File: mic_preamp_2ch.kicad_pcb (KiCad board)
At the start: 2 copper layers, 100 x 78 mm, 47 parts, among them J1 NC3FAH1, J2 NC3FAH1, J3 PWR +15/GND/-15, J4 P48 +48/GND, J5 OUT1/GND/OUT2/GND, U1 INA163UA, U2 INA163UA

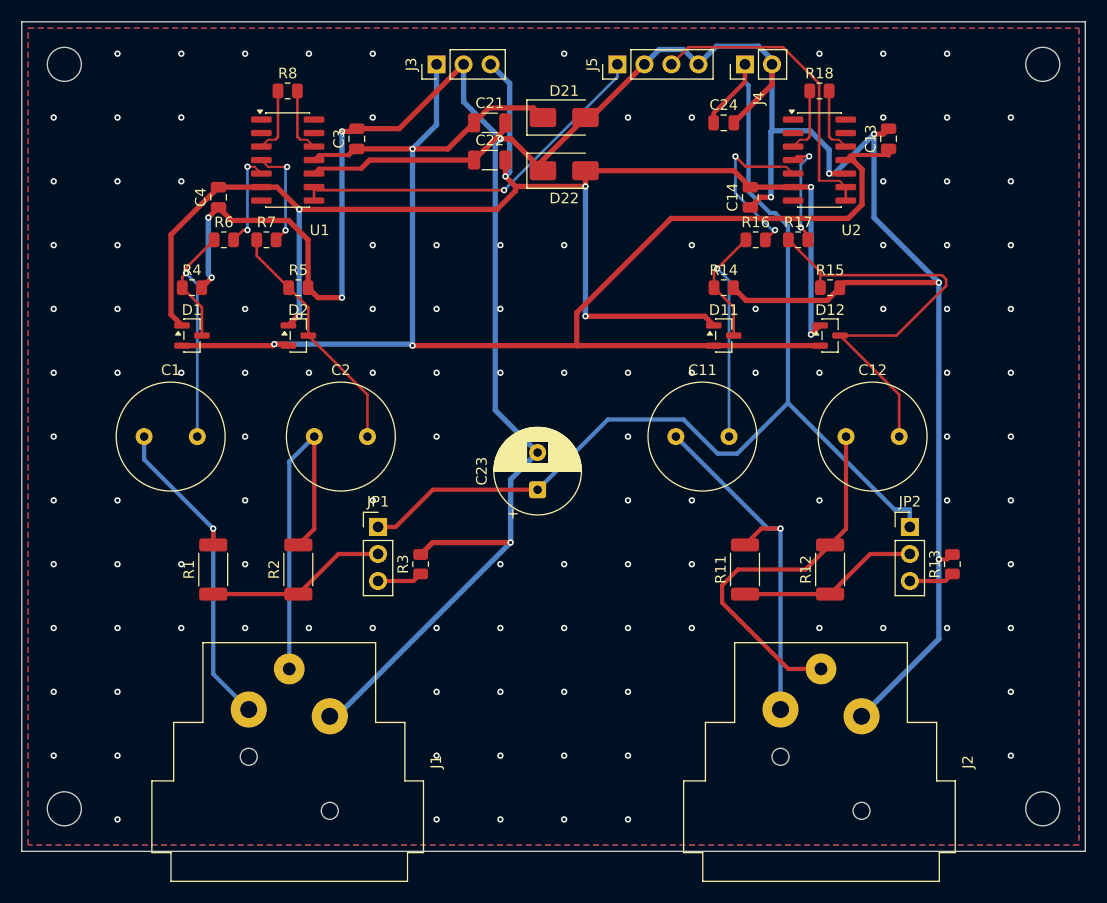
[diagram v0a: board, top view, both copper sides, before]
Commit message: v2: hand-routed symmetric input path, 0.1% matched parts, 10R series
Fixes the review of efc1e58: the 47R series resistors were a misreading of
datasheet Fig.2 (47R is in parallel with 1.2uH there) and doubled input noise.
Phantom feed is now 2x3.40k 0.1% per leg, bias 2.2k 0.1%, series 10R.
Input legs are routed by hand and locked; only power/phantom/GND autorouted.
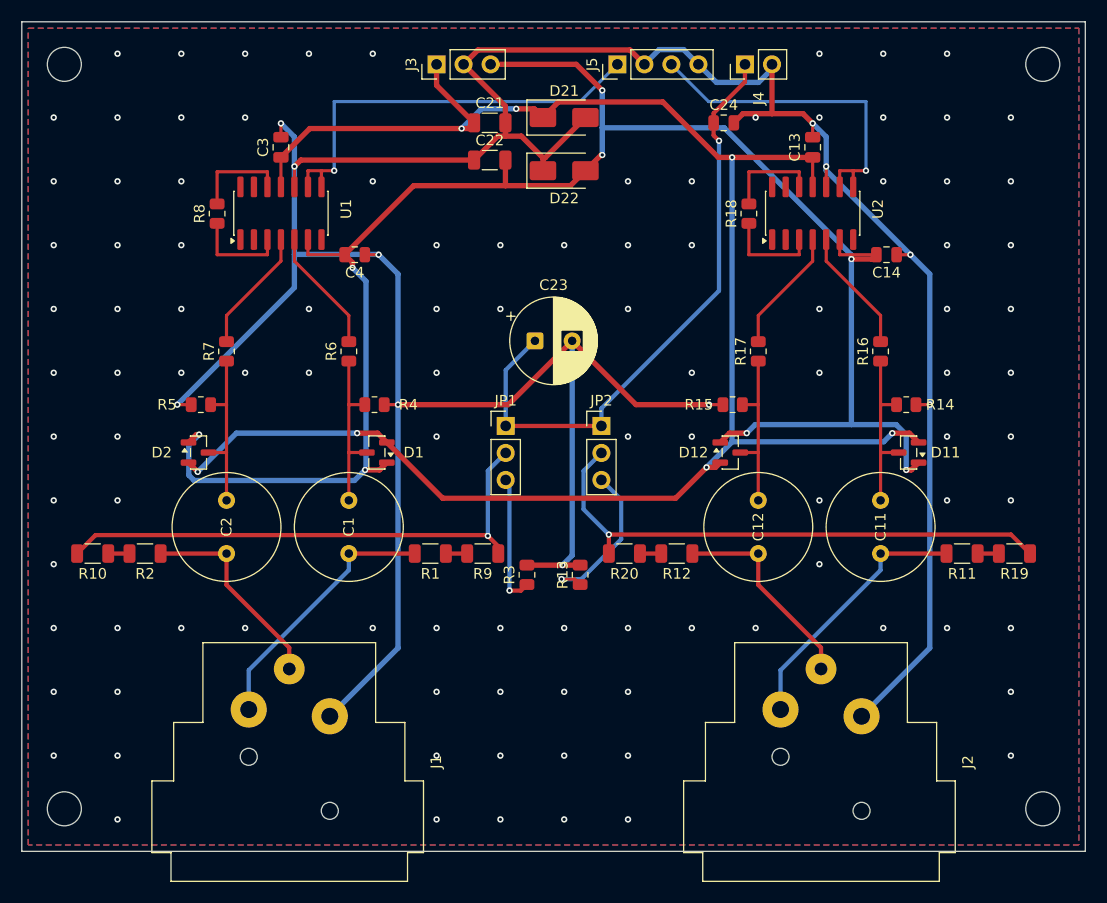
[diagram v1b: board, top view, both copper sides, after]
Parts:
- added R10: 3.40k, Resistor_SMD:R_1206_3216Metric, F.Cu at (6.66, 50.0)
- added R19: 3.40k, Resistor_SMD:R_1206_3216Metric, F.Cu at (93.3, 50.0)
- added R20: 3.40k, Resistor_SMD:R_1206_3216Metric, F.Cu at (56.7, 50.0)
- added R9: 3.40k, Resistor_SMD:R_1206_3216Metric, F.Cu at (43.3, 50.0)
- R1, R11, R12, R2: value 6.81k -> 3.40k; footprint Resistor_SMD:R_2010_5025Metric -> Resistor_SMD:R_1206_3216Metric
- R16, R17, R6, R7: value 47R -> 10R
- moved R13 35.0 mm to (52.5, 52.0)
- moved JP2 30.5 mm to (54.5, 38.0)
- moved C1 22.2 mm to (30.8, 50.0), turned to 90 degrees
- moved C11 22.2 mm to (80.8, 50.0), turned to 90 degrees
- moved D1 20.6 mm to (33.4, 40.5), turned to 180 degrees
- moved D11 20.6 mm to (83.4, 40.5), turned to 180 degrees
- moved R1 20.5 mm to (38.4, 50.0), turned to 180 degrees
- moved R11 20.5 mm to (88.4, 50.0), turned to 180 degrees
- moved R4 20.4 mm to (33.2, 36.0)
- moved R14 20.4 mm to (83.2, 36.0)
- moved R16 15.7 mm to (80.8, 31.0), turned to 90 degrees
- moved R6 15.7 mm to (30.8, 31.0), turned to 90 degrees
- moved JP1 15.3 mm to (45.5, 38.0)
- moved R12 14.5 mm to (61.6, 50.0), turned to 0 degrees
- moved R2 14.5 mm to (11.6, 50.0), turned to 0 degrees
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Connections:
- R1 pad 1: /PH1 -> /P1H
- R11 pad 1: /PH2 -> /P2H
- R12 pad 1: /PH2 -> /P2C
- R2 pad 1: /PH1 -> /P1C
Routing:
- net /+48V: track 103.8 -> 58.2 mm, vias 0 -> 1
- net /PH2: track 17.1 -> 51.5 mm, vias 0 -> 1
- net /-15V: track 141.1 -> 174.2 mm, vias 7 -> 8
- net /PH1: track 17.1 -> 49.9 mm, vias 0 -> 1
- net /IN2N_PROT: track 42.1 -> 16.3 mm
- net /XLR2_COLD: track 36.1 -> 19.5 mm
- net /+15V: track 156.9 -> 173.1 mm, vias 3 -> 7
- net /XLR1_COLD: track 33.6 -> 19.5 mm
- net /P48OFF2: track 4.28 -> 15.5 mm, vias 0 -> 1
- net /IN2P_PROT: track 27.3 -> 16.3 mm, vias 1 -> 0
- net /IN1P_PROT: track 26.8 -> 16.3 mm, vias 1 -> 0
- net /XLR2_HOT: track 34.4 -> 24.8 mm, vias 1 -> 0
- net /P48OFF1: track 4.28 -> 12.4 mm, vias 0 -> 1
- net /IN1N_PROT: track 22.8 -> 16.3 mm
- net /XLR1_HOT: track 31.3 -> 24.8 mm, vias 1 -> 0
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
